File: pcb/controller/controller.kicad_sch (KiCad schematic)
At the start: 32 parts, among them J1 Conn_01x03, J2 Conn_01x03, J3 RELAY_CONN, J4 Remote_header, J5 PWR_IN, J6 MFRC_CONN, J7 Micro_SD_Card, J8 Conn_01x03, J9 Conn_01x03, Q1 MMBT3906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

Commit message: Update to kicad10 format
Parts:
- U1, U2: value ~ -> (none)

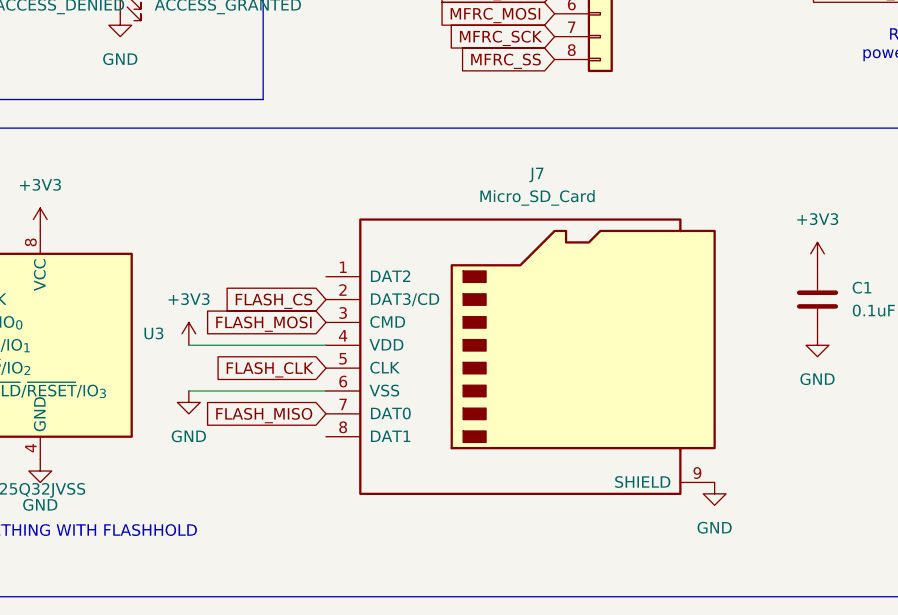
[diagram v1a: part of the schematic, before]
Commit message: Change footprint to use through-hole, add Edge.cuts cutout for debug pins.
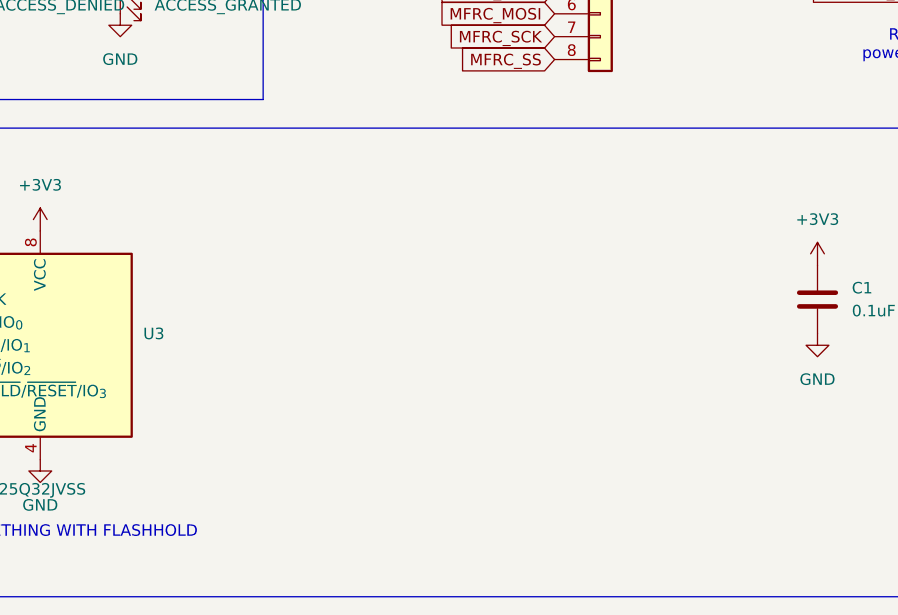
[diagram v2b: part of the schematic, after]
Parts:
- removed J7: Micro_SD_Card, Connector_Card:microSD_HC_Molex_104031-0811, symbol Connector:Micro_SD_Card
- A1: footprint Module:RaspberryPi_Pico_SMD_HandSolder -> Module:RaspberryPi_Pico_Common_Unspecified
